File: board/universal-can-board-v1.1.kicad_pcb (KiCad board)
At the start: 2 copper layers, 49.3 x 59.4 mm, 77 parts, among them IC1 ATMEGA328P-A, P1 USB_OTG, P2 CONN_01X08, P3 CONN_01X02, P4 CONN_01X08, P5 CONN_01X08, SW1 SW_Push, U1 FT232RL, U2 LM1117-3.3, U3 MCP2515-I/ST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

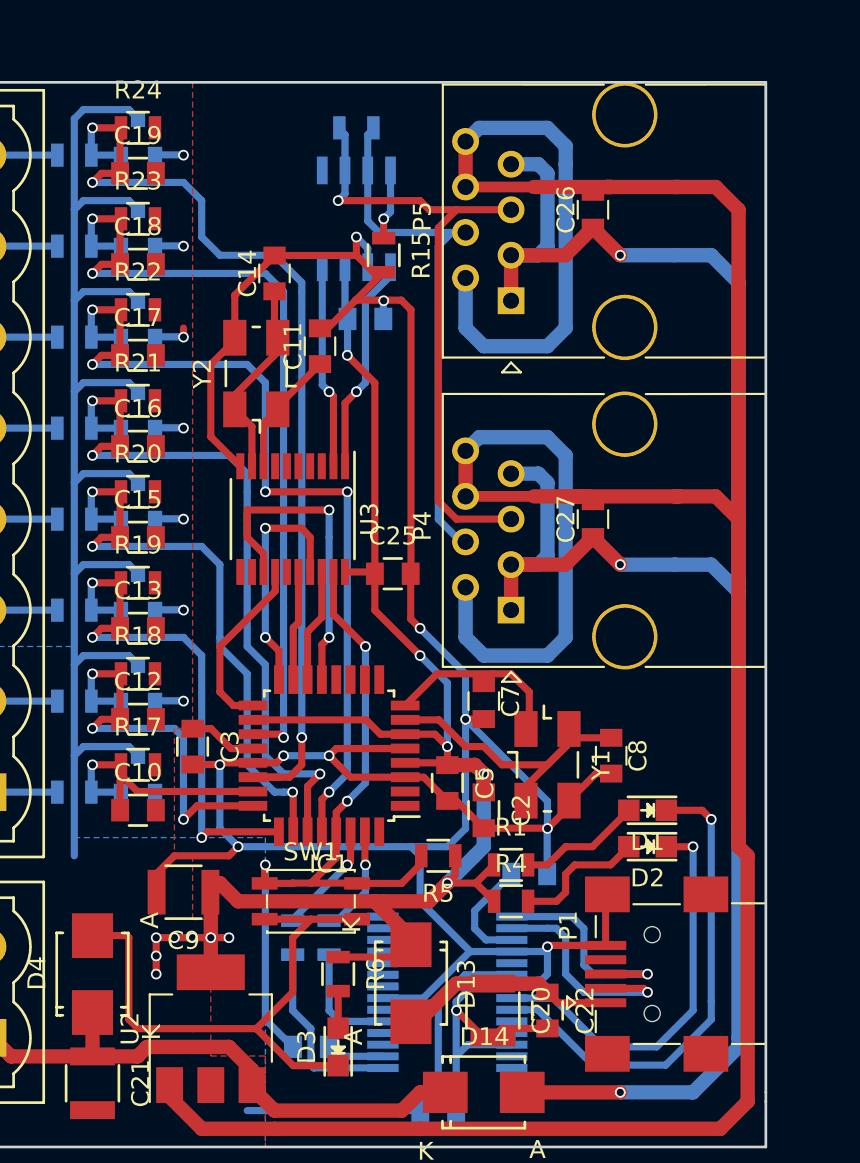
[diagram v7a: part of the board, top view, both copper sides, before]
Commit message: Added two mounting holes to the pcb.
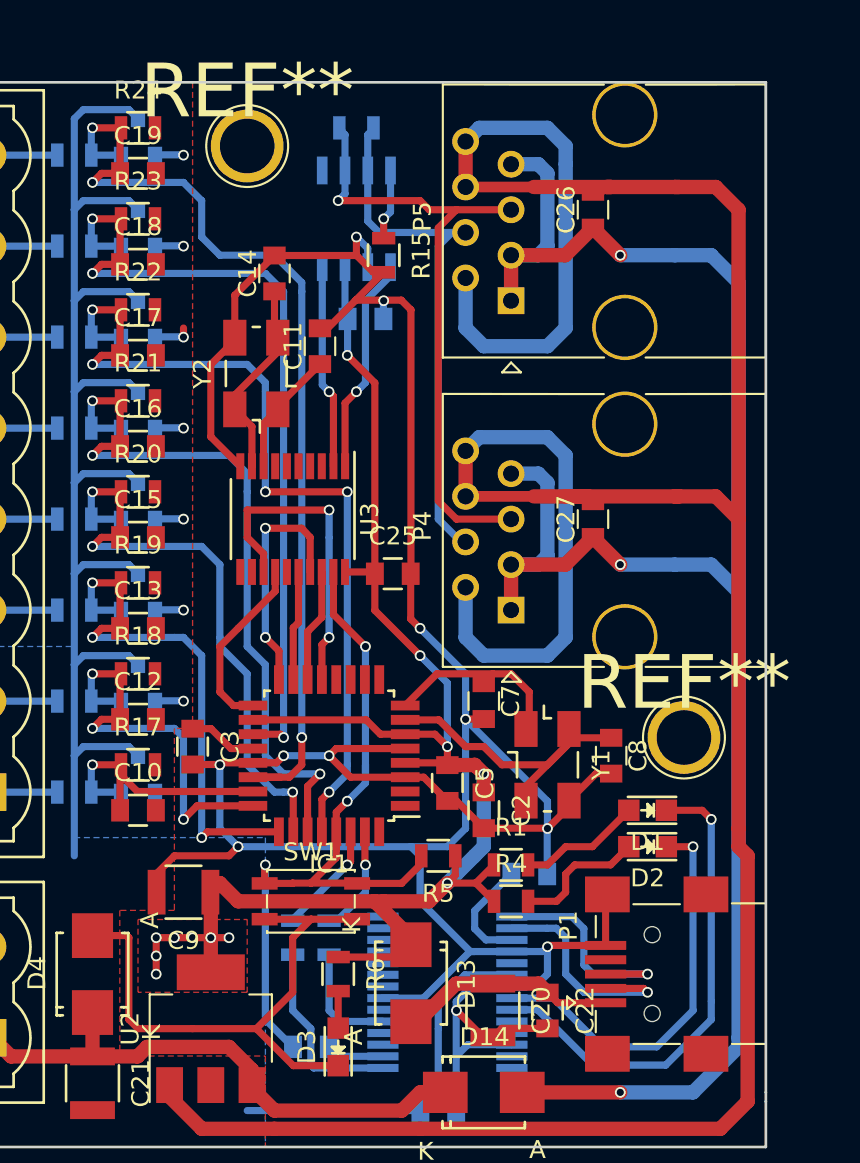
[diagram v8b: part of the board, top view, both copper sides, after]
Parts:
- added REF**: 1pin, Connectors:1pin, F.Cu at (165.6, 87.4)
- added REF**: 1pin, Connectors:1pin, F.Cu at (141.2, 54.4)
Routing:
- added copper zone on F.Cu, net VCC
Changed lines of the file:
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@@
     (tracks 752)
     (zones 0)
-    (modules 77)
+    (modules 79)
     (nets 79)
   )
@@
     (uvia_drill 0.1)
   )
+  (module Connectors:1pin (layer F.Cu)
+    (at 165.608 87.376)
+    (descr "module 1 pin (ou trou mecanique de percage)")
+    (tags DEV)
+    (fp_text reference REF** (at 0 -3.048) (layer F.SilkS)
+      (effects (font (size 3 3) (thickness 0.15)))
+    )
+    (fp_text value 1pin (at 0 3) (layer F.Fab)
+      (effects (font (size 1 1) (thickness 0.15)))
+    )
+    (fp_circle (center 0 0) (end 2 0.8) (layer F.Fab) (width 0.1))
+    (fp_circle (center 0 0) (end 2.6 0) (layer F.CrtYd) (width 0.05))
+    (fp_circle (center 0 0) (end 0 -2.286) (layer F.SilkS) (width 0.12))
+    (pad 1 thru_hole circle (at 0 0) (size 4.064 4.064) (drill 3.048) (layers *.Cu *.Mask))
+  )
   (module Buttons_Switches_SMD:SW_SPST_EVQP2 (layer F.Cu)
     (at 144.78 96.52)
@@
     )
   )
+  (module Connectors:1pin (layer F.Cu)
+    (at 141.224 54.356)
+    (descr "module 1 pin (ou trou mecanique de percage)")
+    (tags DEV)
+    (fp_text reference REF** (at 0 -3.048) (layer F.SilkS)
+      (effects (font (size 3 3) (thickness 0.15)))
+    )
+    (fp_text value 1pin (at 0 3) (layer F.Fab)
+      (effects (font (size 1 1) (thickness 0.15)))
+    )
+    (fp_circle (center 0 0) (end 2 0.8) (layer F.Fab) (width 0.1))
+    (fp_circle (center 0 0) (end 2.6 0) (layer F.CrtYd) (width 0.05))
+    (fp_circle (center 0 0) (end 0 -2.286) (layer F.SilkS) (width 0.12))
+    (pad 1 thru_hole circle (at 0 0) (size 4.064 4.064) (drill 3.048) (layers *.Cu *.Mask))
+  )
   (gr_line (start 121.92 50.8) (end 120.904 50.8) (angle 90) (layer Edge.Cuts) (width 0.15))
   (gr_line (start 120.904 110.236) (end 120.904 50.8) (angle 90) (layer Edge.Cuts) (width 0.15))
@@
   (segment (start 138.176 103.632) (end 135.128 103.632) (width 0.4) (layer F.Cu) (net 2))
   (segment (start 141.732 103.632) (end 138.176 103.632) (width 0.4) (layer F.Cu) (net 2))
-  (segment (start 134.50316 98.43516) (end 132.588 98.43516) (width 0.4) (layer F.Cu) (net 2) (status 800000))
+  (segment (start 134.50316 98.43516) (end 132.588 98.43516) (width 0.4) (layer F.Cu) (net 2))
   (segment (start 134.62 98.552) (end 134.50316 98.43516) (width 0.4) (layer F.Cu) (net 2))
   (segment (start 134.62 103.124) (end 134.62 98.552) (width 0.4) (layer F.Cu) (net 2))
@@
   (segment (start 139.208 86.884) (end 140.316 87.992) (width 0.4) (layer F.Cu) (net 4))
   (segment (start 140.316 87.992) (end 141.546 87.992) (width 0.4) (layer F.Cu) (net 4))
-  (segment (start 143.78 104.648) (end 143.764 104.648) (width 0.4) (layer B.Cu) (net 5) (status C00000))
-  (segment (start 143.764 104.648) (end 142.24 103.124) (width 0.4) (layer B.Cu) (net 5) (status 400000))
-  (segment (start 142.2 94.528) (end 142.2 95.52) (width 0.4) (layer F.Cu) (net 5) (status 800000))
+  (segment (start 143.78 104.648) (end 143.764 104.648) (width 0.4) (layer B.Cu) (net 5))
+  (segment (start 143.764 104.648) (end 142.24 103.124) (width 0.4) (layer B.Cu) (net 5))
+  (segment (start 142.2 94.528) (end 142.2 95.52) (width 0.4) (layer F.Cu) (net 5))
   (segment (start 142.24 94.488) (end 142.2 94.528) (width 0.4) (layer F.Cu) (net 5))
   (via (at 142.24 94.488) (size 0.6) (drill 0.4) (layers F.Cu B.Cu) (net 5))
@@
     (polygon
       (pts
-        (xy 138.176 86.868) (xy 137.16 86.868) (xy 137.16 93.98) (xy 138.176 93.98) (xy 138.176 97.536)
-        (xy 139.192 97.536) (xy 139.192 105.156) (xy 142.24 105.156) (xy 142.24 110.236) (xy 120.904 110.236)
-        (xy 120.904 50.8) (xy 138.176 50.8)
+        (xy 138.176 86.868) (xy 137.16 86.868) (xy 137.16 93.98) (xy 137.16 97.028) (xy 134.112 97.028)
+        (xy 134.112 105.156) (xy 142.24 105.156) (xy 142.24 110.236) (xy 120.904 110.236) (xy 120.904 50.8)
+        (xy 138.176 50.8)
       )
     )
@@
       )
     )
+  )
+  (zone (net 3) (net_name VCC) (layer F.Cu) (hatch edge 0.508)
+    (connect_pads (clearance 0.508))
+    (min_thickness 0.254)
+    (fill yes (arc_segments 16) (thermal_gap 0.508) (thermal_bridge_width 0.508))
+    (polygon
+      (pts
+        (xy 141.224 101.6) (xy 135.128 101.6) (xy 135.128 97.536) (xy 141.224 97.536)
+      )
+    )
